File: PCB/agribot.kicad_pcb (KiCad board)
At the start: 2 copper layers, 260 x 149.6 mm, 100 parts, among them J1 M1_PWR, J10 NEMA17_Conn_1x04, J11 NEO6M_GPS, J12 MDD10A_Signal, J13 MDD10A_Signal, J14 MicroSD_Conn_1x06, J15 spare audio pins, J16 spare sensor pins, J2 M2_PWR, J3 SOIL_PROBE_PWR, J4 Screw_Terminal_01x02, J5 XT60, J6 XT60, J7 Conn_01x03_Pin, J8 Conn_01x03_Pin, J9 AHT20_BMP280_Conn_1x04, M1 Motor_Servo, M2 Motor_Servo, M3 LM2596S_Module, M4 LM2596S_Module, M5 LM2596S_Module, M6 LM2596S_Module, M7 LM2596S_Module, M8 MAX485_Auto_Module, U1 Display link (CYD), U10 ESP32 DevKit 30-pin, U11 ESP32 DevKit 30-pin, U12 ESP32 DevKit 30-pin, U2 ultrasonic, U3 ultrasonic, U4 BH1750_GY302_Module, U5 MPU6050_GY521, U6 MAX98357A_Module, U7 MAX98357A_Module, U8 SIM800L_Module, U9 DRV8825_Carrier

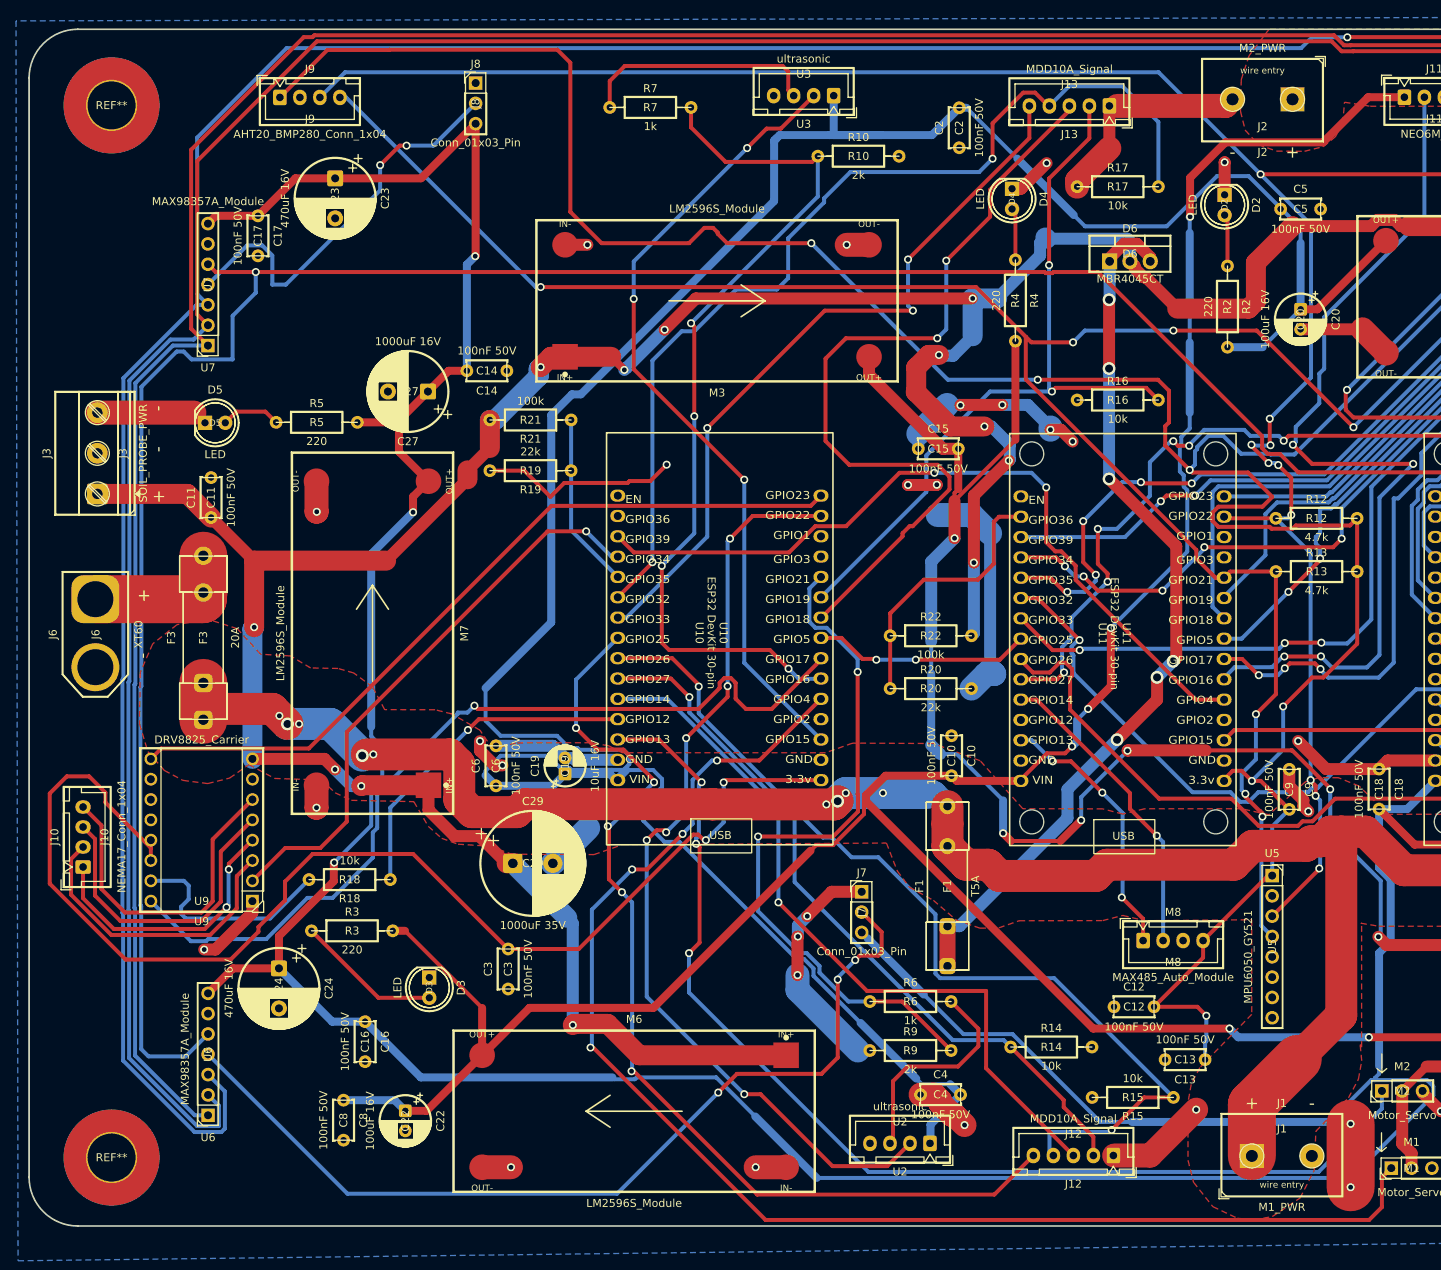
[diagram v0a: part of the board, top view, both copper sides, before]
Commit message: Board: moved M2_PWR, reroute, zones refilled
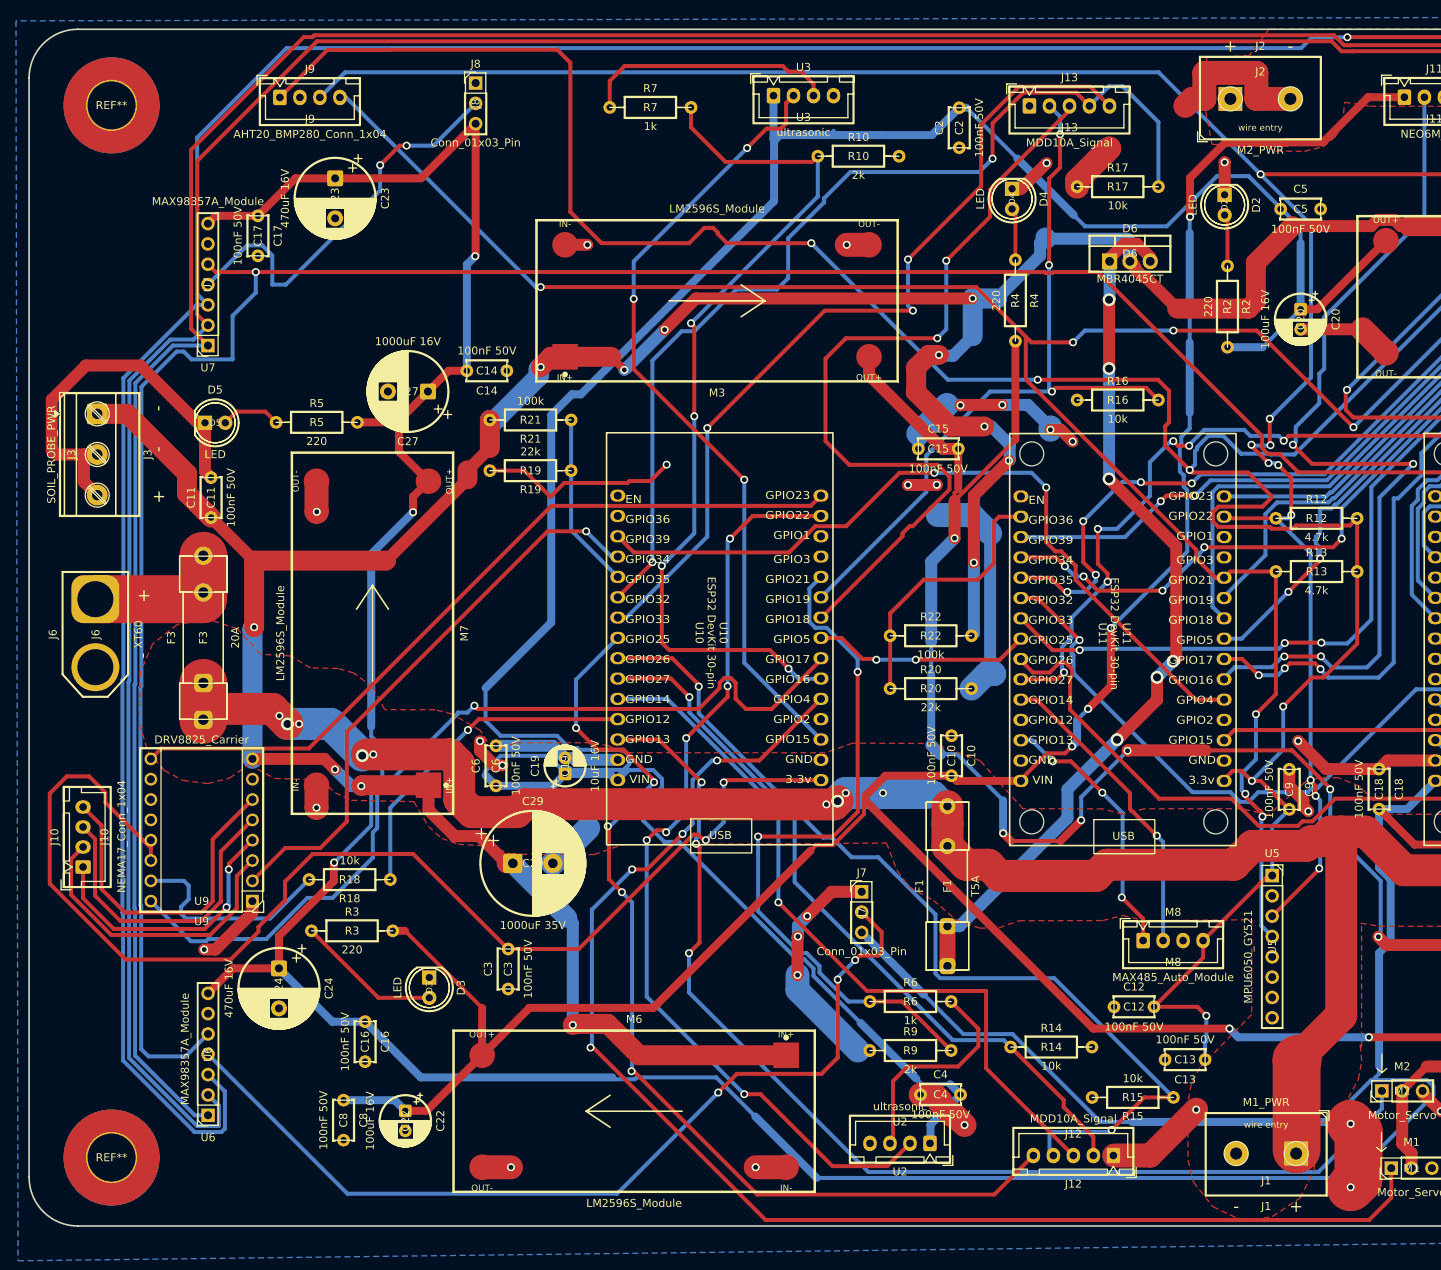
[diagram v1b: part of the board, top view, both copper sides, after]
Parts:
- moved J3 10.0 mm to (30.4, 62.2), turned to -90 degrees
- moved J13 9.99 mm to (147.0, 23.7), turned to 0 degrees
- moved J2 7.76 mm to (172.1, 22.8), turned to 0 degrees
- moved U3 7.52 mm to (115.0, 22.4), turned to 0 degrees
- moved J1 5.55 mm to (180.3, 154.6), turned to 180 degrees
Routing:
- net /GND: track 386.5 -> 423.4 mm
- net Net-(J13-DIR1): track 92.9 -> 107.2 mm
- net /12v: track 455.0 -> 460.6 mm
- net /5V (main): track 353.2 -> 349.5 mm
- net /12v_RAW: track 528.4 -> 525.2 mm
- net Net-(U3-echo): track 30.0 -> 31.9 mm
- net /15: track 100.5 -> 99.5 mm
- net /19: track 94.3 -> 93.8 mm, vias 2 -> 3

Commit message: LM2596 footprint fix: correct pin order + pitch, rerouted
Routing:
- net /12v: track 460.6 -> 511.3 mm, vias 12 -> 16
- net /GND: track 423.4 -> 386.8 mm, vias 33 -> 47
- net /4v(SIM): track 246.0 -> 274.9 mm, vias 6 -> 8
- net /5V (servo): track 195.9 -> 215.5 mm, vias 5 -> 7
- net /5v(A): track 678.9 -> 690.6 mm
- net /5v(S): track 471.6 -> 481.1 mm
- net /LRCLK: track 488.6 -> 495.2 mm
- net /12v_RAW: track 525.2 -> 521.8 mm
- net /5V (main): track 349.5 -> 350.9 mm
- net Net-(J12-DIR1): track 124.7 -> 125.7 mm

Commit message: Board cleanup: remove dangling stubs, name mounting holes H1-H4, move SIM800L note off silkscreen
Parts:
- renumbered REF** to H1, REF** to H2, REF** to H3, REF** to H4
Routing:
- net /GND: track 386.8 -> 361.1 mm
- net /12v: track 511.3 -> 502.7 mm
- net /5V (main): track 350.9 -> 350.2 mm
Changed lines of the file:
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@@
 			)
 		)
-		(fp_text user "rows 21.6 / offset 2.42 - measure"
-			(at 10.8 16.4 0)
-			(layer "F.SilkS")
-			(effects
-				(font
-					(size 0.7 0.7)
-					(thickness 0.1)
-				)
-			)
-		)
 		(fp_text user "${REFERENCE}"
 			(at 10.8 1 0)
@@
 			)
 		)
+		(fp_text user "rows 21.6 / offset 2.42 - measure"
+			(at 10.8 16.4 0)
+			(layer "F.Fab")
+			(effects
+				(font
+					(size 0.7 0.7)
+					(thickness 0.1)
+				)
+			)
+		)
 		(pad "1" thru_hole rect
 			(at 0 0 180)
@@
 		(descr "Mounting Hole 6mm, generated by kicad-footprint-generator mountinghole.py")
 		(tags "mountinghole")
-		(property "Reference" "REF**"
+		(property "Reference" "H2"
 			(at 0 -6.95 0)
 			(layer "F.SilkS")
@@
 		(descr "Mounting Hole 6mm, generated by kicad-footprint-generator mountinghole.py")
 		(tags "mountinghole")
-		(property "Reference" "REF**"
+		(property "Reference" "H1"
 			(at 0 -6.95 0)
 			(layer "F.SilkS")
@@
 		(descr "Mounting Hole 6mm, generated by kicad-footprint-generator mountinghole.py")
 		(tags "mountinghole")
-		(property "Reference" "REF**"
+		(property "Reference" "H4"
 			(at 0 -6.95 0)
 			(layer "F.SilkS")
@@
 		(descr "Mounting Hole 6mm, generated by kicad-footprint-generator mountinghole.py")
 		(tags "mountinghole")
-		(property "Reference" "REF**"
+		(property "Reference" "H3"
 			(at 0 -6.95 0)
 			(layer "F.SilkS")
@@
 	)
 	(segment
-		(start 85.598 57.5056)
-		(end 85.598 56.5912)
-		(width 2.5)
-		(layer "B.Cu")
-		(net "/12v")
-	)
-	(segment
 		(start 244.4912 69.918)
 		(end 240.2912 65.718)
@@
 	)
 	(segment
-		(start 80.1624 62.9412)
-		(end 85.598 57.5056)
-		(width 2.5)
-		(layer "B.Cu")
-		(net "/12v")
-	)
-	(segment
 		(start 137.414 54.9148)
 		(end 135.7376 54.9148)
@@
 	)
 	(segment
-		(start 175.3188 22.8076)
-		(end 179.5688 22.8076)
-		(width 3)
-		(layer "F.Cu")
-		(net "/GND")
-	)
-	(segment
 		(start 87.0712 72.5424)
 		(end 83.806 69.2772)
@@
 	)
 	(segment
-		(start 152.908 33.02)
-		(end 156.9422 28.9858)
-		(width 3)
-		(layer "F.Cu")
-		(net "/GND")
-	)
-	(segment
 		(start 244.9576 19.05)
 		(end 244.2972 18.3896)
@@
 	)
 	(segment
-		(start 168.8188 22.8076)
-		(end 168.8188 19.5576)
-		(width 3)
-		(layer "F.Cu")
-		(net "/GND")
-	)
-	(segment
 		(start 138.8364 151.0792)
 		(end 137.5764 149.8192)
@@
 	)
 	(segment
-		(start 166.4352 23.6872)
-		(end 167.3148 22.8076)
-		(width 3)
-		(layer "F.Cu")
-		(net "/GND")
-	)
-	(segment
 		(start 83.806 69.2772)
 		(end 79.502 69.2772)
@@
 	)
 	(segment
-		(start 175.3188 19.5576)
-		(end 175.3188 22.8076)
-		(width 3)
-		(layer "F.Cu")
-		(net "/GND")
-	)
-	(segment
 		(start 188.0764 157.8716)
 		(end 188.0764 152.364)
@@
 	)
 	(segment
-		(start 167.3148 22.8076)
-		(end 168.8188 22.8076)
-		(width 3)
-		(layer "F.Cu")
-		(net "/GND")
-	)
-	(segment
 		(start 171.346 30.7364)
 		(end 171.3484 30.734)
@@
 	)
 	(segment
-		(start 168.8188 19.5576)
-		(end 175.3188 19.5576)
-		(width 3)
-		(layer "F.Cu")
-		(net "/GND")
-	)
-	(segment
 		(start 122.2248 121.92)
 		(end 119.1768 124.968)
@@
 	)
 	(segment
-		(start 121.9358 27.3304)
-		(end 122.4788 26.7874)
-		(width 0.5)
-		(layer "B.Cu")
-		(net "/5V (main)")
-	)
-	(segment
 		(start 134.7616 27.3304)
 		(end 128.4224 27.3304)
@@
 		(net "Net-(J13-DIR1)")
 	)
-	(segment
-		(start 140.9192 25.8572)
-		(end 140.9192 26.0096)
-		(width 0.5)
-		(layer "F.Cu")
-		(net "Net-(J13-DIR1)")
-	)
 	(via
 		(at 132.3848 49.276)
@@
 	)
 	(segment
-		(start 150.7744 28.6004)
-		(end 150.7744 28.194)
-		(width 0.5)
-		(layer "F.Cu")
-		(net "/19")
-	)
-	(segment
 		(start 150.7744 27.2288)
 		(end 150.7744 28.6004)
@@
 		(net "/GPIO 26")
 	)
-	(segment
-		(start 273.6596 111.2304)
-		(end 273.558 111.332)
-		(width 0.5)
-		(layer "B.Cu")
-		(net "/GPIO 26")
-	)
